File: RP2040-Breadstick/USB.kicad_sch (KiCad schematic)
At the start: 5 parts

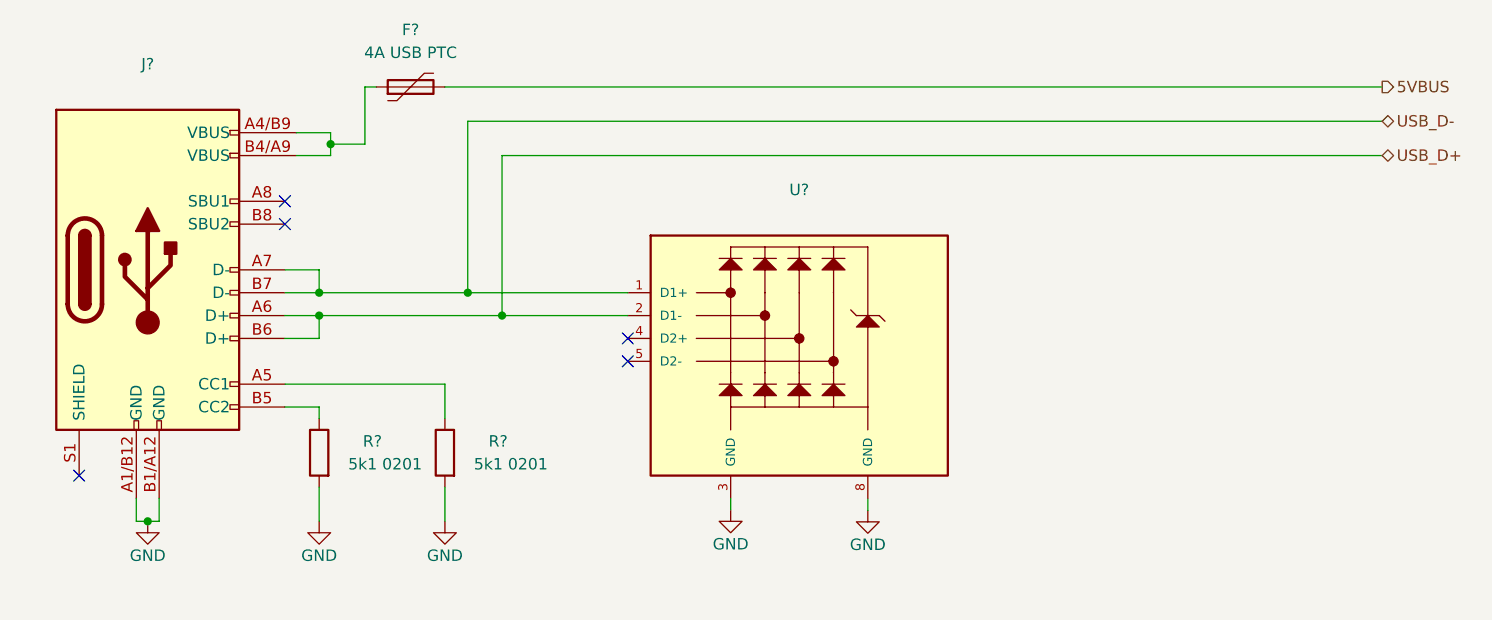
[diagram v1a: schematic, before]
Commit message: Moved schematic changes into PCB
All the changes made in the schematic have been moved into the PCB editor. It was a bit of work due to the amount of reorganizing done in the schematic which led to a lot of new reference numbers. Was easy enough to get most things back into place where they were before.
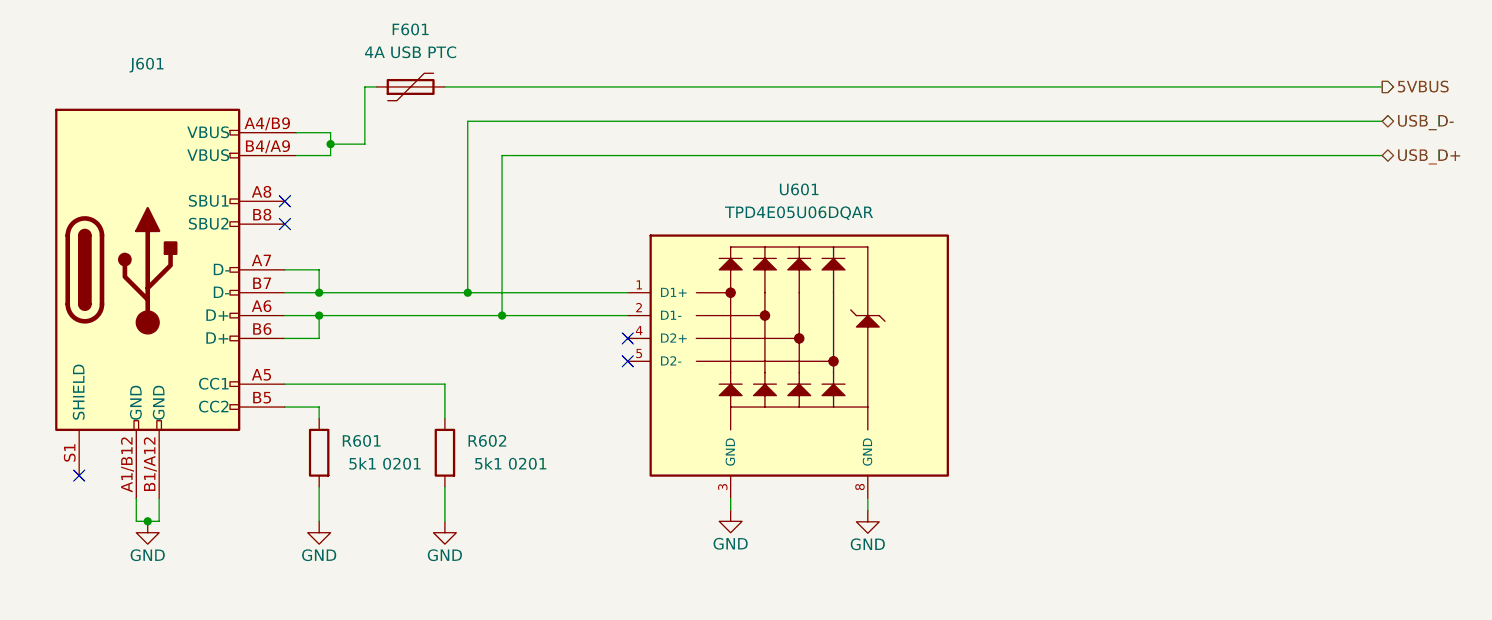
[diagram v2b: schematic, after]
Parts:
- U601: renamed from U?; value (none) -> TPD4E05U06DQAR
- gave numbers to parts that had none: 4
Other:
- company: (none) -> J & R Creative Technologies Inc.
- title: (none) -> Raspberry Breadstick
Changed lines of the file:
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@@
 (kicad_sch (version 20211123) (generator eeschema)
   (paper "A4")
+  (title_block
+    (title "Raspberry Breadstick")
+    (date "2023-07-02")
+    (rev "0.2")
+    (company "J & R Creative Technologies Inc.")
+    (comment 1 "@RangenMichael")
+    (comment 2 "https://twitter.com/RangenMichael")
+    (comment 3 "Apache-2.0 License")
+    (comment 4 "https://github.com/mrangen/Raspberry-Breadstick")
+    (comment 5 "https://shop.breadstick.ca/")
+  )
   (junction (at 109.22 86.36) (diameter 0) (color 0 0 0 0)
   )
@@
   (symbol (lib_id "power:GND") (at 153.67 127 0) (unit 1)
     (in_bom yes) (on_board yes)
-    (property "Reference" "#PWR?" (id 0) (at 153.67 133.35 0)
+    (property "Reference" "#PWR0604" (id 0) (at 153.67 133.35 0)
       (effects (font (size 1.27 1.27)) hide)
     )
@@
   (symbol (lib_id "power:GND") (at 107.95 128.27 0) (unit 1)
     (in_bom yes) (on_board yes)
-    (property "Reference" "#PWR?" (id 0) (at 107.95 134.62 0)
+    (property "Reference" "#PWR0602" (id 0) (at 107.95 134.62 0)
       (effects (font (size 1.27 1.27)) hide)
     )
@@
   (symbol (lib_id "Device:R") (at 107.95 120.65 0) (mirror y) (unit 1)
     (in_bom yes) (on_board yes)
-    (property "Reference" "R?" (id 0) (at 114.935 119.38 0)
+    (property "Reference" "R601" (id 0) (at 114.935 119.38 0)
       (effects (font (size 1.27 1.27)) (justify left))
     )
@@
   (symbol (lib_id "TPD4E05U06DQAR:TPD4E05U06DQAR") (at 161.29 106.68 0) (unit 1)
     (in_bom yes) (on_board yes) (fields_autoplaced)
-    (property "Reference" "U?" (id 0) (at 161.29 91.44 0))
-    (property "Value" "" (id 1) (at 161.29 93.98 0))
+    (property "Reference" "U601" (id 0) (at 161.29 91.44 0))
+    (property "Value" "TPD4E05U06DQAR" (id 1) (at 161.29 93.98 0))
     (property "Footprint" "TI_TPD4E05U06DQAR" (id 2) (at 161.29 106.68 0)
       (effects (font (size 1.27 1.27)) (justify left bottom) hide)
@@
   (symbol (lib_id "Device:Polyfuse") (at 118.11 80.01 90) (unit 1)
     (in_bom yes) (on_board yes) (fields_autoplaced)
-    (property "Reference" "F?" (id 0) (at 118.11 73.66 90))
+    (property "Reference" "F601" (id 0) (at 118.11 73.66 90))
     (property "Value" "4A USB PTC" (id 1) (at 118.11 76.2 90))
     (property "Footprint" "Fuse:Fuse_0805_2012Metric" (id 2) (at 123.19 78.74 0)
@@
   (symbol (lib_id "power:GND") (at 88.9 128.27 0) (unit 1)
     (in_bom yes) (on_board yes)
-    (property "Reference" "#PWR?" (id 0) (at 88.9 134.62 0)
+    (property "Reference" "#PWR0601" (id 0) (at 88.9 134.62 0)
       (effects (font (size 1.27 1.27)) hide)
     )
@@
   (symbol (lib_id "Device:R") (at 121.92 120.65 0) (mirror y) (unit 1)
     (in_bom yes) (on_board yes)
-    (property "Reference" "R?" (id 0) (at 128.905 119.38 0)
+    (property "Reference" "R602" (id 0) (at 128.905 119.38 0)
       (effects (font (size 1.27 1.27)) (justify left))
     )
@@
   (symbol (lib_id "power:GND") (at 168.91 127.0589 0) (unit 1)
     (in_bom yes) (on_board yes)
-    (property "Reference" "#PWR?" (id 0) (at 168.91 133.4089 0)
+    (property "Reference" "#PWR0605" (id 0) (at 168.91 133.4089 0)
       (effects (font (size 1.27 1.27)) hide)
     )
@@
   (symbol (lib_id "Connector:USB_C_Receptacle_USB2.0") (at 88.9 100.33 0) (unit 1)
     (in_bom yes) (on_board yes) (fields_autoplaced)
-    (property "Reference" "J?" (id 0) (at 88.9 77.47 0))
+    (property "Reference" "J601" (id 0) (at 88.9 77.47 0))
     (property "Value" "" (id 1) (at 88.9 80.01 0))
     (property "Footprint" "" (id 2) (at 92.71 100.33 0)
@@
   (symbol (lib_id "power:GND") (at 121.92 128.27 0) (unit 1)
     (in_bom yes) (on_board yes)
-    (property "Reference" "#PWR?" (id 0) (at 121.92 134.62 0)
-      (effects (font (size 1.27 1.27)) hide)
-    )
+    (property "Reference" "#PWR0603" (id 0) (at 121.92 134.62 0)
+      (effects (font (size 1.27 1.27)) hide)
+    )

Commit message: Started routing power and LEDs
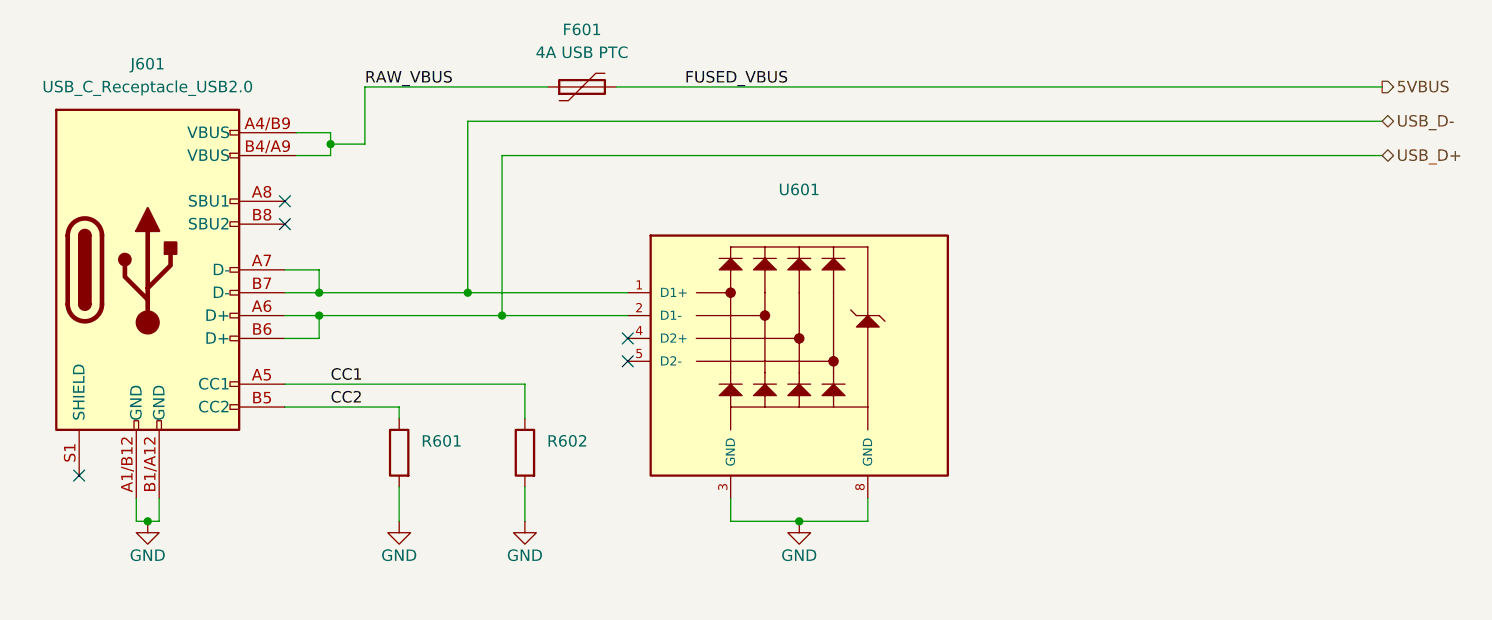
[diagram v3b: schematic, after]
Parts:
- J601: value (none) -> USB_C_Receptacle_USB2.0; footprint (none) -> USB-C Molex:USB-C-2171790001
- R601, R602: value 5k1 0201 -> (none); footprint _Breadstick_Footprints:Perfect_0201_Resistor -> (none)
- U601: value TPD4E05U06DQAR -> (none)
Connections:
- net GND: now also U601.8 (GND)
- net USB_D-: now also U601.10 (NC)
- net CC2: now reaches J601.B5 (CC2), R601.1
- net at U601.4 (D2+): now also U601.7 (NC)
- net at U601.5 (D2-): now also U601.6 (NC)
- net RAW_VBUS: now reaches F601.1, J601.A4/B9 (VBUS), J601.B4/A9 (VBUS)
- net CC1: now reaches J601.A5 (CC1), R602.1
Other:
- moved on the sheet: F601, R601, R602

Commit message: working on rev0.2 still
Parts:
- R601, R602: value (none) -> 5k1 0603; footprint (none) -> Resistor_SMD:R_0603_1608Metric
- U601: value (none) -> TPD4E05U06DQAR
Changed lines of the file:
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@@
       (effects (font (size 1.27 1.27)) (justify left))
     )
-    (property "Value" "" (id 1) (at 128.27 121.92 0)
+    (property "Value" "5k1 0603" (id 1) (at 128.27 121.92 0)
       (effects (font (size 1.27 1.27)) (justify left))
     )
-    (property "Footprint" "" (id 2) (at 118.618 120.65 90)
+    (property "Footprint" "Resistor_SMD:R_0603_1608Metric" (id 2) (at 118.618 120.65 90)
       (effects (font (size 1.27 1.27)) hide)
     )
@@
     (in_bom yes) (on_board yes) (fields_autoplaced)
     (property "Reference" "U601" (id 0) (at 161.29 91.44 0))
-    (property "Value" "" (id 1) (at 161.29 93.98 0))
+    (property "Value" "TPD4E05U06DQAR" (id 1) (at 161.29 93.98 0))
     (property "Footprint" "TI_TPD4E05U06DQAR" (id 2) (at 161.29 106.68 0)
       (effects (font (size 1.27 1.27)) (justify left bottom) hide)
@@
       (effects (font (size 1.27 1.27)) (justify left))
     )
-    (property "Value" "" (id 1) (at 142.24 121.92 0)
+    (property "Value" "5k1 0603" (id 1) (at 142.24 121.92 0)
       (effects (font (size 1.27 1.27)) (justify left))
     )
-    (property "Footprint" "" (id 2) (at 132.588 120.65 90)
+    (property "Footprint" "Resistor_SMD:R_0603_1608Metric" (id 2) (at 132.588 120.65 90)
       (effects (font (size 1.27 1.27)) hide)
     )

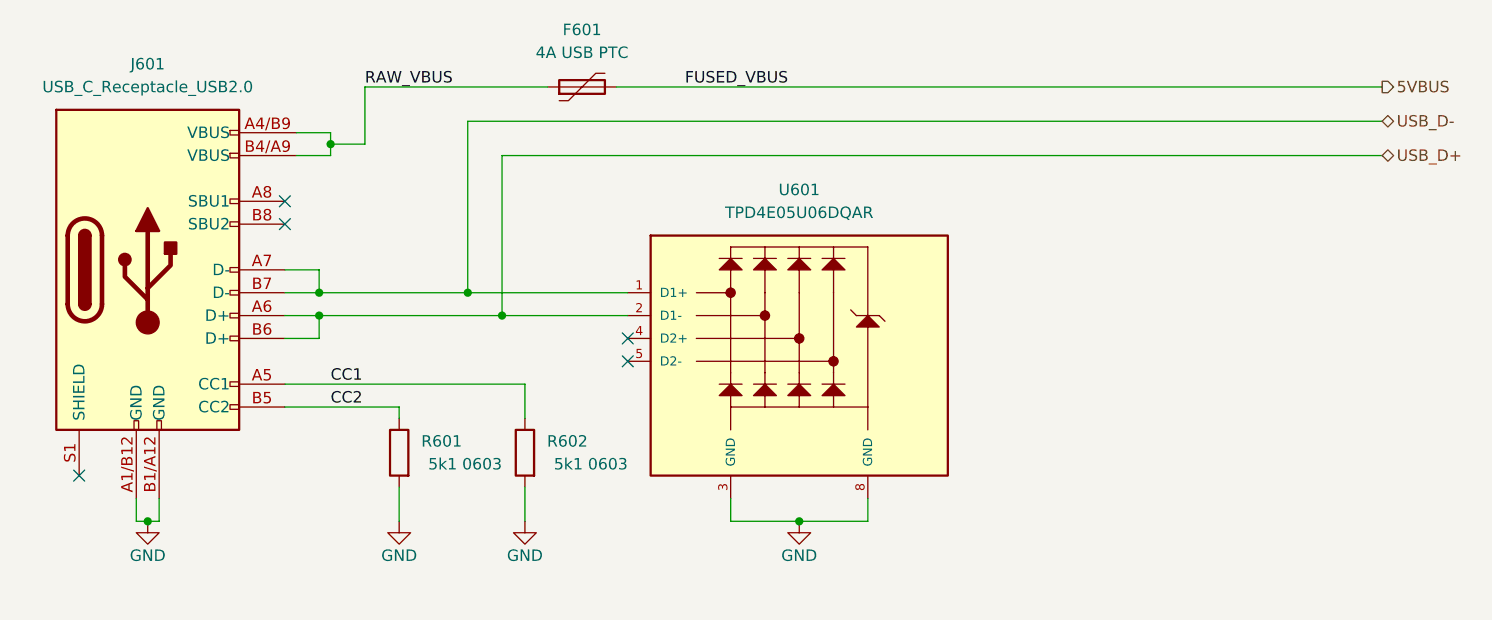
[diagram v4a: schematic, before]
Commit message: Finished assigning I/O pins, perfect is the enemy of good.
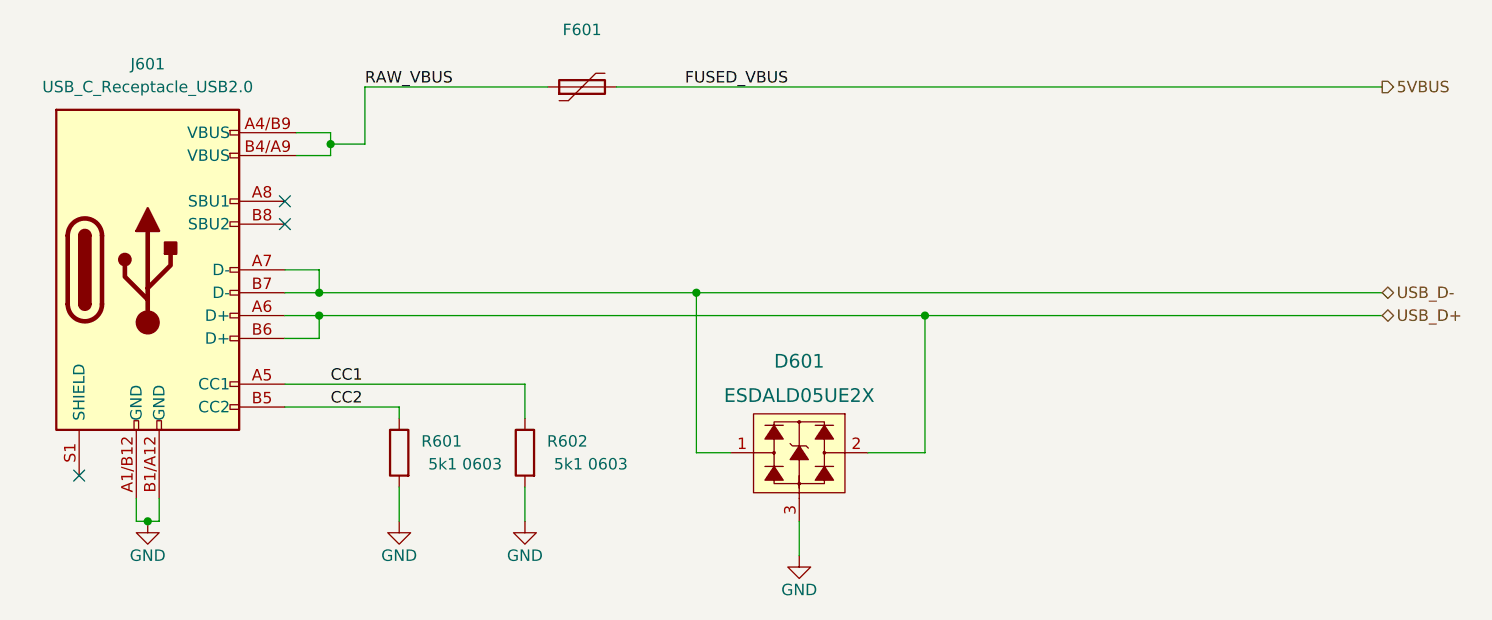
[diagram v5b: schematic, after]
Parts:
- removed U601: TPD4E05U06DQAR, TI_TPD4E05U06DQAR, symbol TPD4E05U06DQAR:TPD4E05U06DQAR
- added D601: ESDALD05UE2X, Package_TO_SOT_SMD:SOT-23, symbol dk_TVS-Diodes:TPD2EUSB30DRTR
- F601: value 4A USB PTC -> (none); footprint Fuse:Fuse_0805_2012Metric -> (none); Digikey 283-PTSLR08058V400DKR-ND -> PTSLR12066V300
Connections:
- net GND: now also D601.3
- net USB_D+: now also D601.2
- net USB_D-: now also D601.1
- no-connect marks 5 -> 3

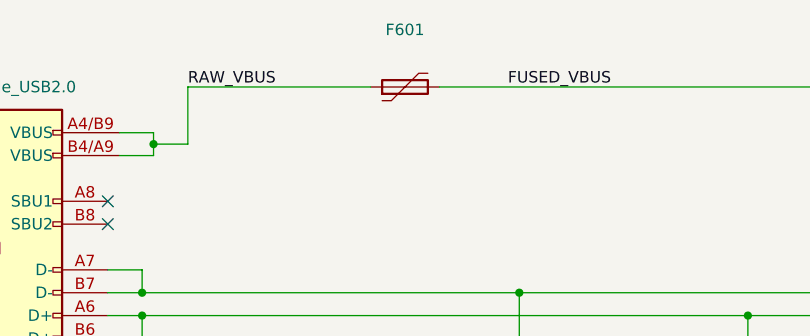
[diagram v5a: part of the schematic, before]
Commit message: replaced switches, upsized some passives to 0603
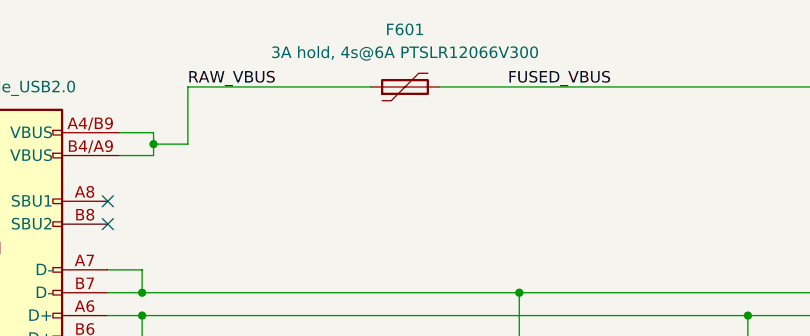
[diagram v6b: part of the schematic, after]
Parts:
- F601: value (none) -> 3A hold, 4s@6A PTSLR12066V300; footprint (none) -> Fuse:Fuse_1206_3216Metric
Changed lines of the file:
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@@
     (in_bom yes) (on_board yes) (fields_autoplaced)
     (property "Reference" "F601" (id 0) (at 137.16 73.66 90))
-    (property "Value" "" (id 1) (at 137.16 76.2 90))
-    (property "Footprint" "" (id 2) (at 142.24 78.74 0)
+    (property "Value" "3A hold, 4s@6A PTSLR12066V300" (id 1) (at 137.16 76.2 90))
+    (property "Footprint" "Fuse:Fuse_1206_3216Metric" (id 2) (at 142.24 78.74 0)
       (effects (font (size 1.27 1.27)) (justify left) hide)
     )
